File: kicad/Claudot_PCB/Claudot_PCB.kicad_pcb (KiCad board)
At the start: 2 copper layers, 104.8 x 57.2 mm, 31 parts, among them J1 Conn_01x12, SW1 SW_Push, SW10 SW_Push, SW11 SW_Push, SW12 SW_Push, SW2 SW_Push, SW3 SW_Push, SW4 SW_Push, SW5 SW_Push, SW6 SW_Push, SW7 SW_Push, SW8 SW_Push, SW9 SW_Push

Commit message: WIP
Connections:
- J1 pad 12: +3V3 -> GND
- J1 pad 2: unconnected-(J1-Pin_2-Pad2) -> +3V3
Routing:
- net GND: vias 94 -> 95
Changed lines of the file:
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@@
 	(net 22 "Net-(D12-A)")
 	(net 23 "unconnected-(J1-Pin_3-Pad3)")
-	(net 24 "unconnected-(J1-Pin_2-Pad2)")
 	(footprint "MountingHole:MountingHole_2.2mm_M2_Pad"
 		(layer "F.Cu")
@@
 			(layers "B.Cu" "B.Mask" "B.Paste")
 			(roundrect_rratio 0.1666666667)
-			(net 24 "unconnected-(J1-Pin_2-Pad2)")
+			(net 21 "+3V3")
 			(pinfunction "Pin_2")
 			(pintype "passive")
@@
 			(layers "B.Cu" "B.Mask" "B.Paste")
 			(roundrect_rratio 0.1666666667)
-			(net 21 "+3V3")
+			(net 20 "GND")
 			(pinfunction "Pin_12")
 			(pintype "passive")
@@
 	)
 	(gr_arc
-		(start 138.175528 75.096166)
-		(mid 138.114281 74.788263)
-		(end 138.09375 74.475)
-		(stroke
-			(width 0.2)
-			(type solid)
-		)
-		(layer "B.Cu")
-		(net 9)
-	)
-	(gr_arc
 		(start 119.615 53.898)
 		(mid 119.322107 54.605107)
@@
 	)
 	(gr_line
-		(start 138.175528 75.096159)
-		(end 138.189082 75.148535)
-		(stroke
-			(width 0.2)
-			(type default)
-		)
-		(layer "B.Cu")
-		(net 9)
-	)
-	(gr_line
 		(start 112.47125 90.17)
 		(end 112.47125 91.998)
@@
 		(net 8)
 	)
+	(gr_line
+		(start 137.74375 79.8985)
+		(end 137.74375 78.1485)
+		(stroke
+			(width 0.2)
+			(type solid)
+		)
+		(layer "B.Cu")
+		(net 20)
+	)
 	(gr_arc
 		(start 128.8625 77.1)
@@
 	(gr_line
 		(start 138.24375 79.8985)
-		(end 138.270862 75.7697)
+		(end 138.24375 75.7697)
 		(stroke
 			(width 0.2)
@@
 	)
 	(gr_arc
-		(start 138.189084 75.148535)
-		(mid 138.250331 75.456438)
-		(end 138.270862 75.769701)
-		(stroke
-			(width 0.2)
-			(type solid)
-		)
-		(layer "B.Cu")
-		(net 9)
-	)
-	(gr_arc
 		(start 114.5245 79.1)
 		(mid 113.110286 78.514214)
@@
 		(net 5)
 	)
+	(gr_line
+		(start 137.64375 78.0485)
+		(end 137.74375 78.1485)
+		(stroke
+			(width 0.2)
+			(type solid)
+		)
+		(layer "B.Cu")
+		(net 20)
+	)
 	(gr_arc
 		(start 51.802625 60.05)
@@
 		(layers "F.Cu" "B.Cu")
 		(remove_unused_layers yes)
+		(keep_end_layers yes)
+		(zone_layer_connections)
+		(net 20)
+	)
+	(via
+		(at 137.64375 78.0485)
+		(size 0.6)
+		(drill 0.3)
+		(layers "F.Cu" "B.Cu")
+		(remove_unused_layers yes)

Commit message: fix: correct row/column net labels
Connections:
- net ROW3 renamed COL3
- net ROW4 renamed COL4
- D1 pad 1: COL0 -> ROW0
- D10 pad 1: COL2 -> ROW2
- D11 pad 1: COL2 -> ROW2
- D12 pad 1: COL2 -> ROW2
- D2 pad 1: COL0 -> ROW0
- D3 pad 1: COL0 -> ROW0
- D4 pad 1: COL0 -> ROW0
- D5 pad 1: COL0 -> ROW0
- D6 pad 1: COL1 -> ROW1
- D7 pad 1: COL1 -> ROW1
- D8 pad 1: COL1 -> ROW1
- D9 pad 1: COL1 -> ROW1
- J1 pad 10: ROW1 -> COL1
- J1 pad 11: ROW0 -> COL0
- J1 pad 4: COL2 -> ROW2
- J1 pad 5: COL1 -> ROW1
- J1 pad 6: COL0 -> ROW0
- J1 pad 9: ROW2 -> COL2
- SW1 pad 1: ROW0 -> COL0
- SW10 pad 1: ROW0 -> COL0
- SW11 pad 1: ROW1 -> COL1
- SW12 pad 1: ROW2 -> COL2
- SW2 pad 1: ROW1 -> COL1
- SW3 pad 1: ROW2 -> COL2
- SW6 pad 1: ROW0 -> COL0
- SW7 pad 1: ROW1 -> COL1
- SW8 pad 1: ROW2 -> COL2
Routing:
- net ROW2: vias 0 -> 4
- net ROW1: vias 0 -> 5
- net ROW0: vias 0 -> 5
- net COL2: vias 4 -> 0
- net COL1: vias 5 -> 0
- net COL0: vias 5 -> 0

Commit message: feat: finalize Claudot_PCB
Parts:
- J1: value Conn_01x12 -> Conn_01x08; footprint Library:AFC01-S12FCC-00 -> Library:AFC01-S08FCC-00
- renumbered D11 to D10, D12 to D11, D5 to D12, D6 to D5, D7 to D6, D8 to D7, D9 to D8, D10 to D9, SW1 to KEY1, SW11 to KEY10, SW12 to KEY11, SW5 to KEY12, SW2 to KEY2, SW3 to KEY3, SW4 to KEY4, SW6 to KEY5, SW7 to KEY6, SW8 to KEY7, SW9 to KEY8, SW10 to KEY9
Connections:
- D12 pad 1: ROW0 -> ROW2
- J1 pad 2: +3V3 -> ROW2
- J1 pad 3: unconnected-(J1-Pin_3-Pad3) -> ROW0
- J1 pad 4: ROW2 -> ROW1
- J1 pad 5: ROW1 -> COL3
- J1 pad 6: ROW0 -> COL2
- J1 pad 7: COL4 -> COL1
- J1 pad 8: COL3 -> COL0
- KEY12 pad 1: COL4 -> COL3
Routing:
- net GND: vias 95 -> 94
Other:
- board text added: "1.0.0+20260208"
- board text removed: "1.0.0+20260117"

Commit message: feat: finalize Claudot_PCB and Claudot_MCU
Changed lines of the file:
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@@
 	(gr_line
 		(start 142.24375 79.3985)
-		(end 142.64375 78.9985)
+		(end 142.668014 78.974236)
 		(stroke
 			(width 0.2)
@@
 	)
 	(via
-		(at 142.64375 78.9985)
+		(at 142.668014 78.974236)
 		(size 0.6)
 		(drill 0.3)

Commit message: chore: complete LCSC part numbers
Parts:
- D1, D10, D11, D12, D2, D3, D4, D5, D6, D7, D8, D9: value D_Small -> 1N4148WS

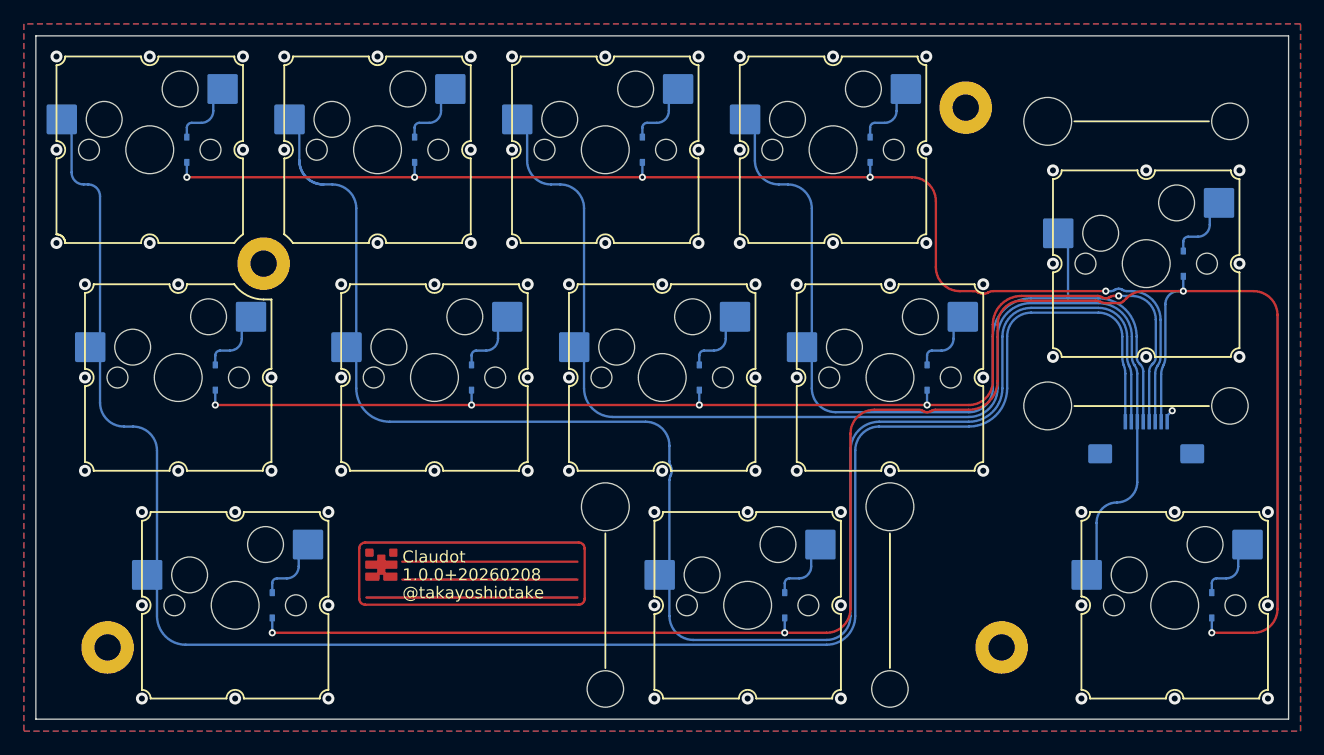
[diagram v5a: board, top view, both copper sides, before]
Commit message: refactor: round pcb corners and adjust silkscreen branding placement
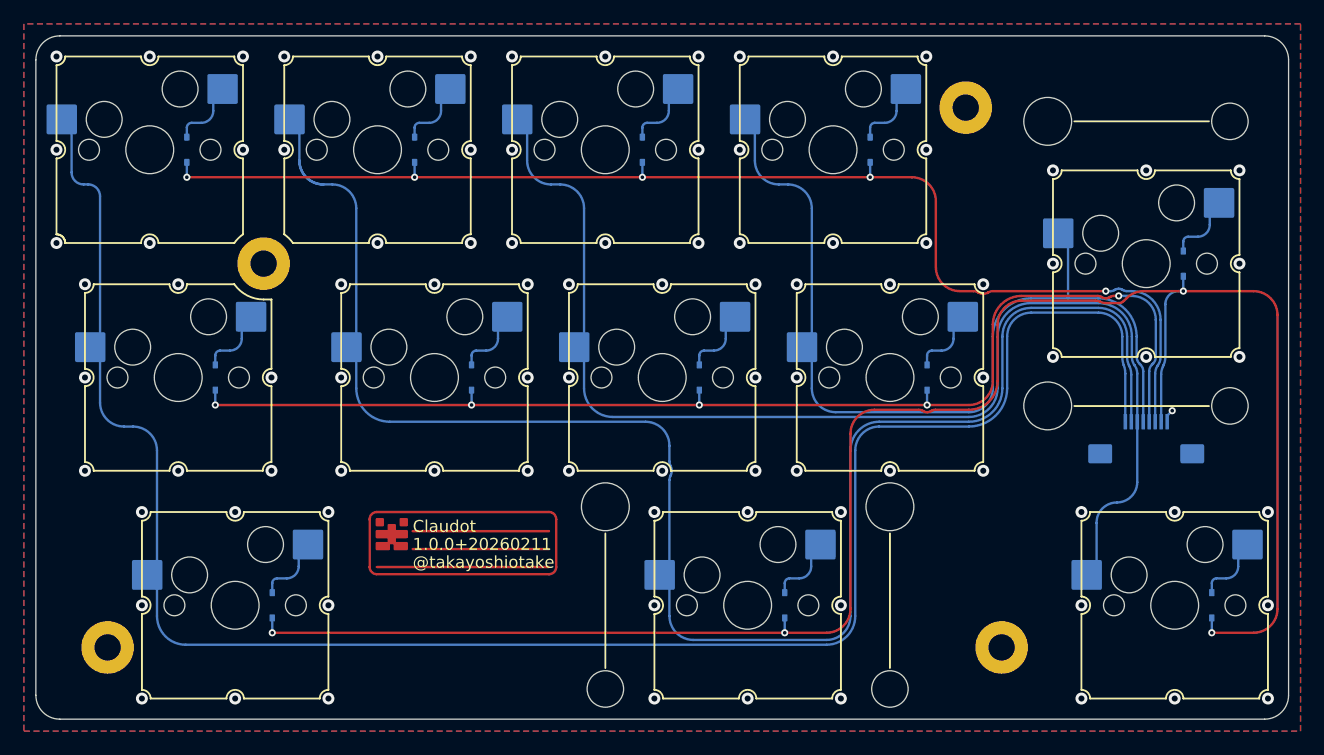
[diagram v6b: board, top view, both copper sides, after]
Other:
- outline, holes or cut-outs redrawn
- board text added: "1.0.0+20260211"
- board text removed: "1.0.0+20260208"
